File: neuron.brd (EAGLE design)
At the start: 61 x 87.6 mm, 123 parts, among them IC1 AD8684RU, IC2 AD8684RU, IC3 ADA4692-2R, IC4 ADA4692-2R, IC5 74HC595D, P30 JUMPER-SMT_3_NO_NO-SILK, P31 JUMPER-SMT_3_NO_NO-SILK, P46 JUMPER-SMT_3_NO_NO-SILK, P47 JUMPER-SMT_3_NO_NO-SILK, SW1 B3U-1000P, U1 TPS72301DBVRSOT-23-5, U2 TLV703, X1 ABM3B-16.000MHZ-B2-T, X2 9HT10-32.768KDZF-T

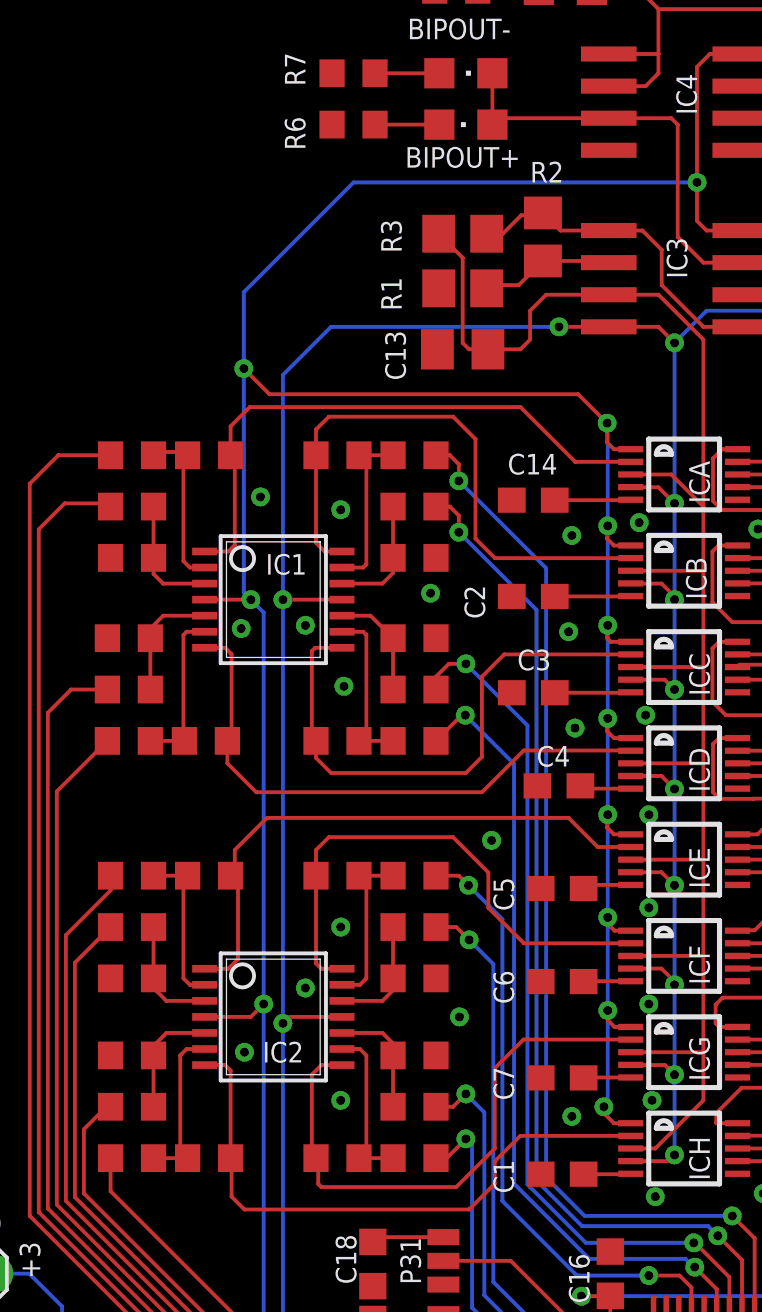
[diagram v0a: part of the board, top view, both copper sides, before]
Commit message: added firmware
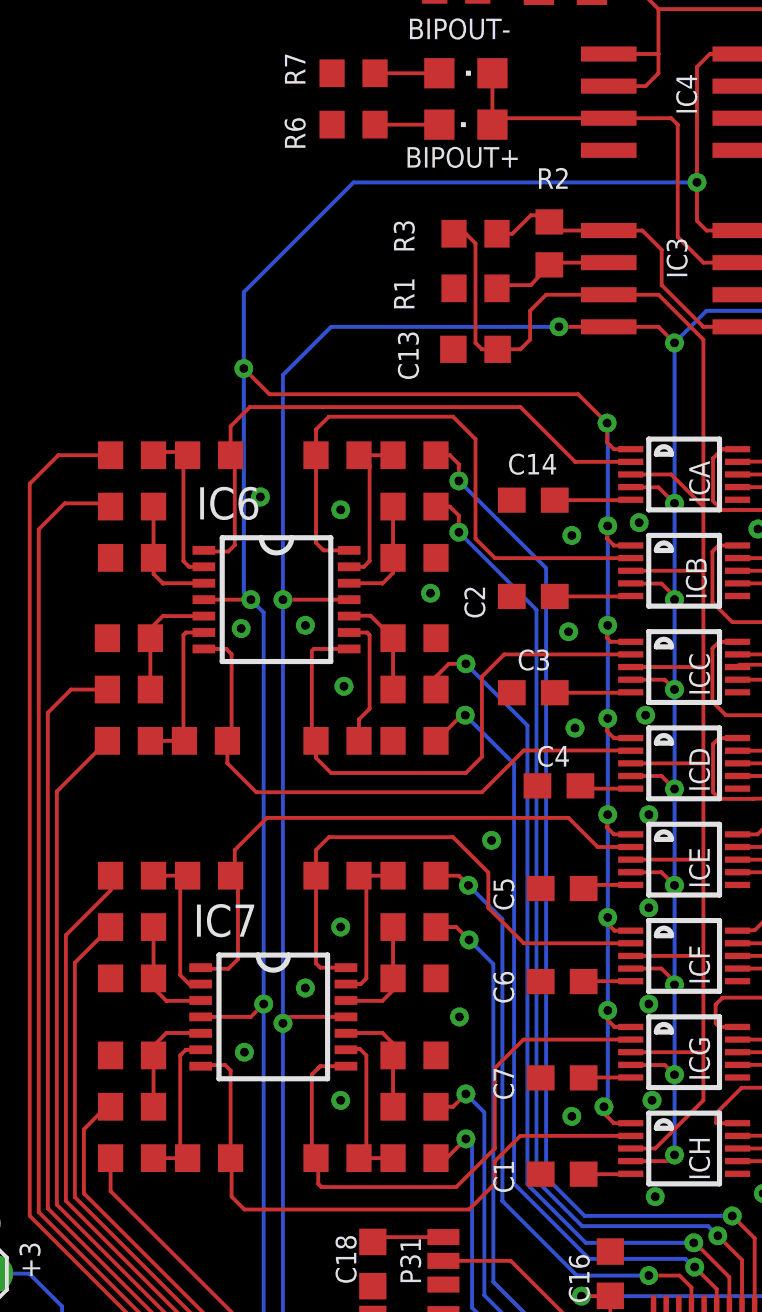
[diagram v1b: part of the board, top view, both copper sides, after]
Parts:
- removed IC1, IC2: AD8684RU, linear:TSSOP14
- added IC6, IC7: AD8609RU, analog-devices:TSSOP14
- C13: device rcl:C0805K -> rcl:C0603K
- C25, C26: value 18p -> 33p
- C27, C28: value 12.5p -> 22p
- R1, R2, R3: device rcl:R0805 -> rcl:R0603
- R4, R5, R6, R7, R8: value 200 -> 180R
- moved C13 0.51 mm to (22.6, 69.6)
- moved R1 0.51 mm to (22.6, 72.0)
- moved R3 0.51 mm to (22.6, 74.2)
- moved R2 0.36 mm to (25.5, 73.8)
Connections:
- removed net N$27: IC2.5, R30.1, R31.1
- new net N$33: IC7.5, R30.1, R31.1
- net +2V5: now also IC6.4, IC7.4; no longer IC1.4, IC2.4
- net -2V5: now also IC6.11, IC7.11; no longer IC1.11, IC2.11
- net AQA: now also IC6.1; no longer IC1.1
- net AQB: now also IC6.14; no longer IC1.14
- net AQC: now also IC6.8; no longer IC1.8
- net AQD: now also IC6.7; no longer IC1.7
- net AQE: now also IC7.1; no longer IC2.1
- net AQF: now also IC7.14; no longer IC2.14
- net AQG: now also IC7.8; no longer IC2.8
- net AQH: now also IC7.7; no longer IC2.7
- net N$15: now also IC6.3; no longer IC1.3
- net N$16: now also IC6.6; no longer IC1.6
- net N$18: now also IC6.10; no longer IC1.10
- net N$19: now also IC6.9; no longer IC1.9
- net N$21: now also IC6.2; no longer IC1.2
- net N$22: now also IC6.12; no longer IC1.12
- net N$23: now also IC6.13; no longer IC1.13
- net N$24: now also IC7.3; no longer IC2.3
- net N$25: now also IC7.12; no longer IC2.12
- net N$26: now also IC6.5; no longer IC1.5
- net N$28: now also IC7.6; no longer IC2.6
- net N$29: now also IC7.10; no longer IC2.10
- net N$30: now also IC7.9; no longer IC2.9
- net N$32: now also IC7.13; no longer IC2.13
- net N$43: now also IC7.2; no longer IC2.2
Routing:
- net N$27: track 4.64 -> 0.00 mm
- net N$33: track 0.00 -> 4.49 mm
- net N$19: track 6.68 -> 5.21 mm
